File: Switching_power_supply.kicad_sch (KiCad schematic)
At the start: 29 parts, among them J8 Conn_01x03_Pin, SW1 SW_DIP_x04, U4 AMS1117, U5 LM2596HVS-ADJRG

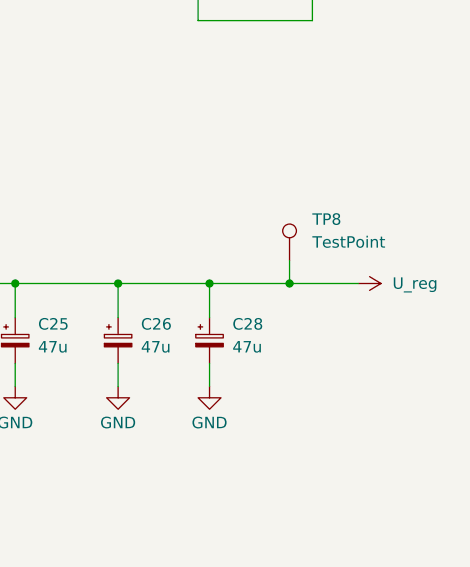
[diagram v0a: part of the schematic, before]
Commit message: ServoController
Dodano arkusz sterownika servo, aktualizacja polaczen
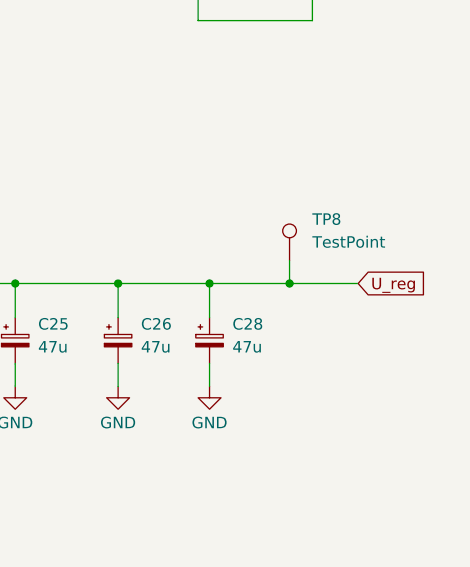
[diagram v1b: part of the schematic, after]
